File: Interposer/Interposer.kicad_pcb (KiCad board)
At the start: 2 copper layers, 55 x 52 mm, 7 parts, among them J1 Conn_01x01_Pin, J10 Conn_01x01_Pin, J11 Conn_01x01_Pin, J2 Conn_01x01_Pin

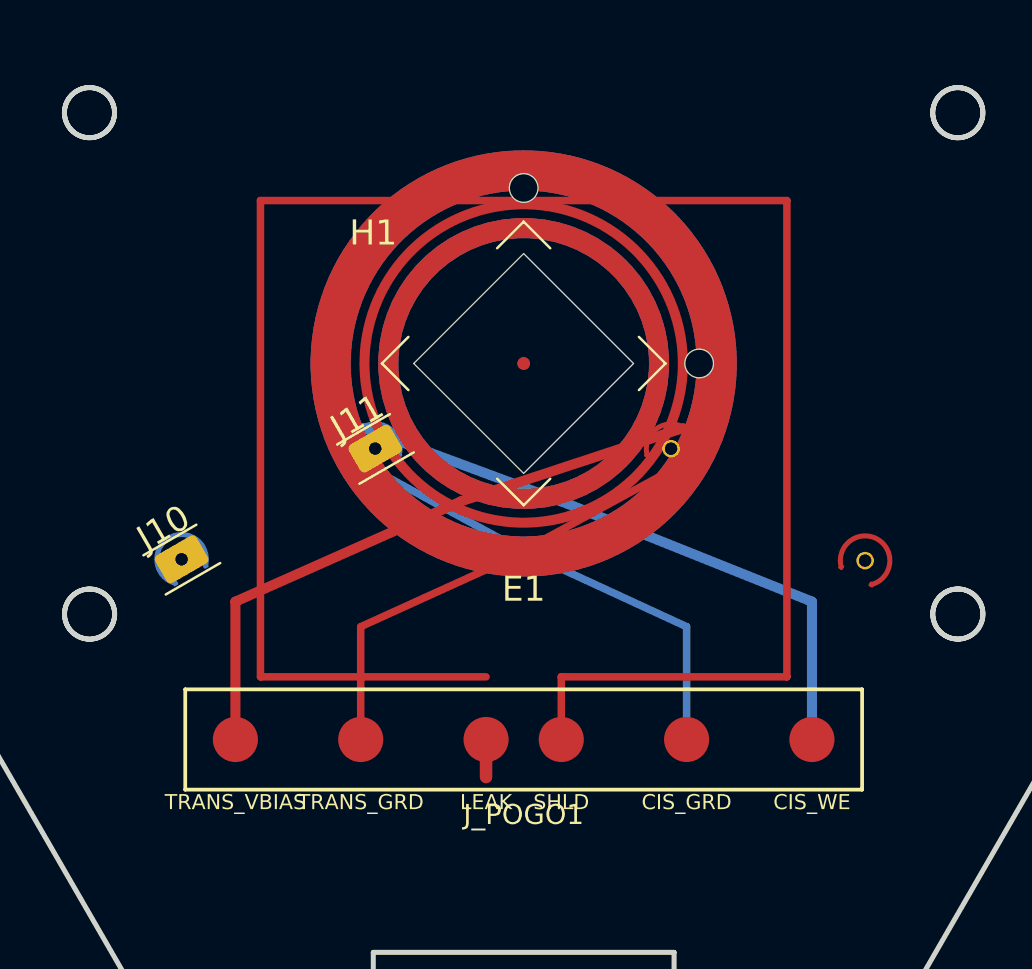
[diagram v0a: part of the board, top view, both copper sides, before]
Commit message: refactor(interposer): reconcile 4-electrode cell with channel-aligned Ag/AgCl ribbons and Gamry pinout
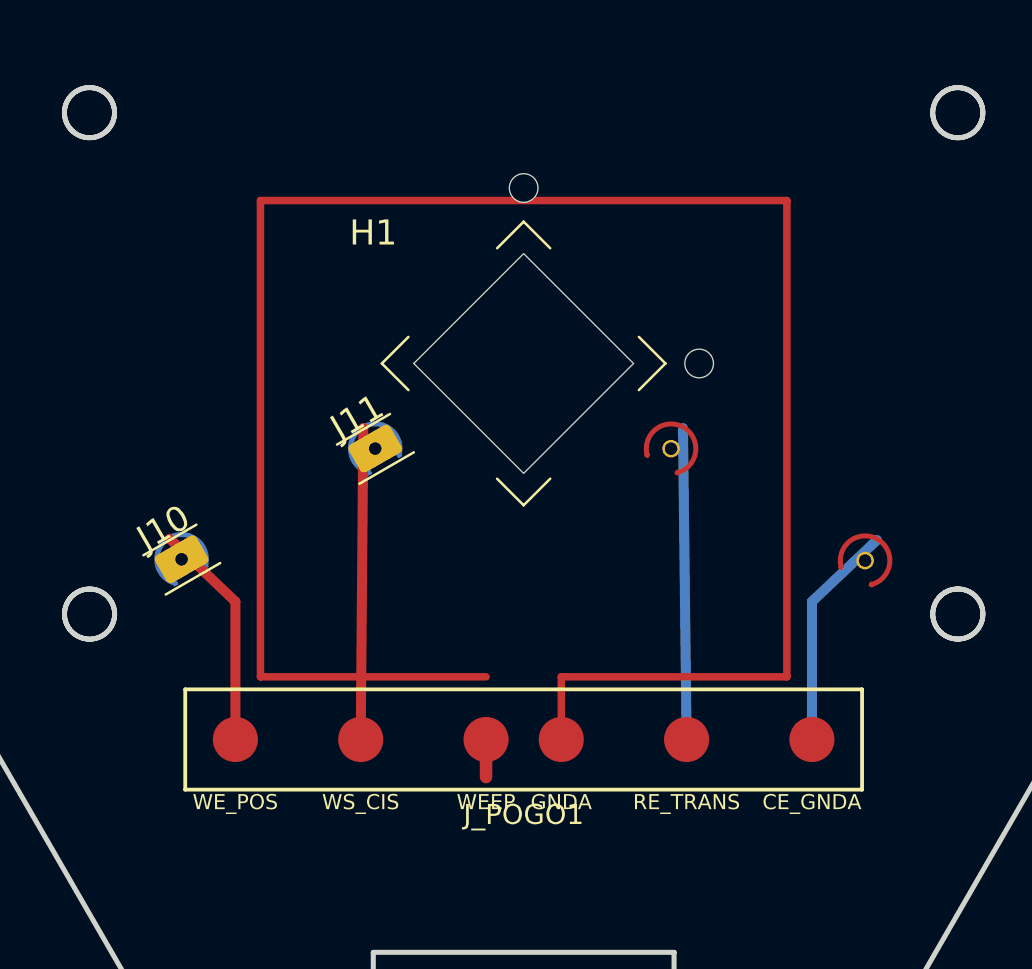
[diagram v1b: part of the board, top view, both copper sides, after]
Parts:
- removed E1: Concentric_Electrode_Cell, footprints:Concentric_Electrode_Cell
- J1: value Conn_01x01_Pin -> RE_TRANS
- J10: value Conn_01x01_Pin -> WE_POS
- J11: value Conn_01x01_Pin -> WS_CIS
- J2: value Conn_01x01_Pin -> CE_GNDA
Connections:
- J1 pad 1: >PORE_AMP -> RE_TRANS
- J1 pad 2: GUARD -> GNDA
- J10 pad 1: Vbias -> WE_POS
- J10 pad 2: GUARD_TRANS -> GNDA
- J11 pad 1: Vbias -> WS_CIS
- J11 pad 2: GUARD_TRANS -> GNDA
- J2 pad 1: >PORE_AMP -> CE_GNDA
- J2 pad 2: GUARD -> GNDA
- J_POGO1 pad 1: >PORE_AMP -> CE_GNDA
- J_POGO1 pad 2: GUARD -> RE_TRANS
- J_POGO1 pad 5: GUARD_TRANS -> WS_CIS
- J_POGO1 pad 6: Vbias -> WE_POS
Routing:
- net Vbias: track 24.7 -> 0.00 mm
- net >PORE_AMP: track 24.7 -> 0.00 mm
- net GUARD_TRANS: track 19.0 -> 0.00 mm
- net GUARD: track 18.9 -> 0.00 mm
- net WS_CIS: track 0.00 -> 12.4 mm
- net RE_TRANS: track 0.00 -> 12.4 mm
- net WE_POS: track 0.00 -> 9.13 mm
- net CE_GNDA: track 0.00 -> 9.07 mm

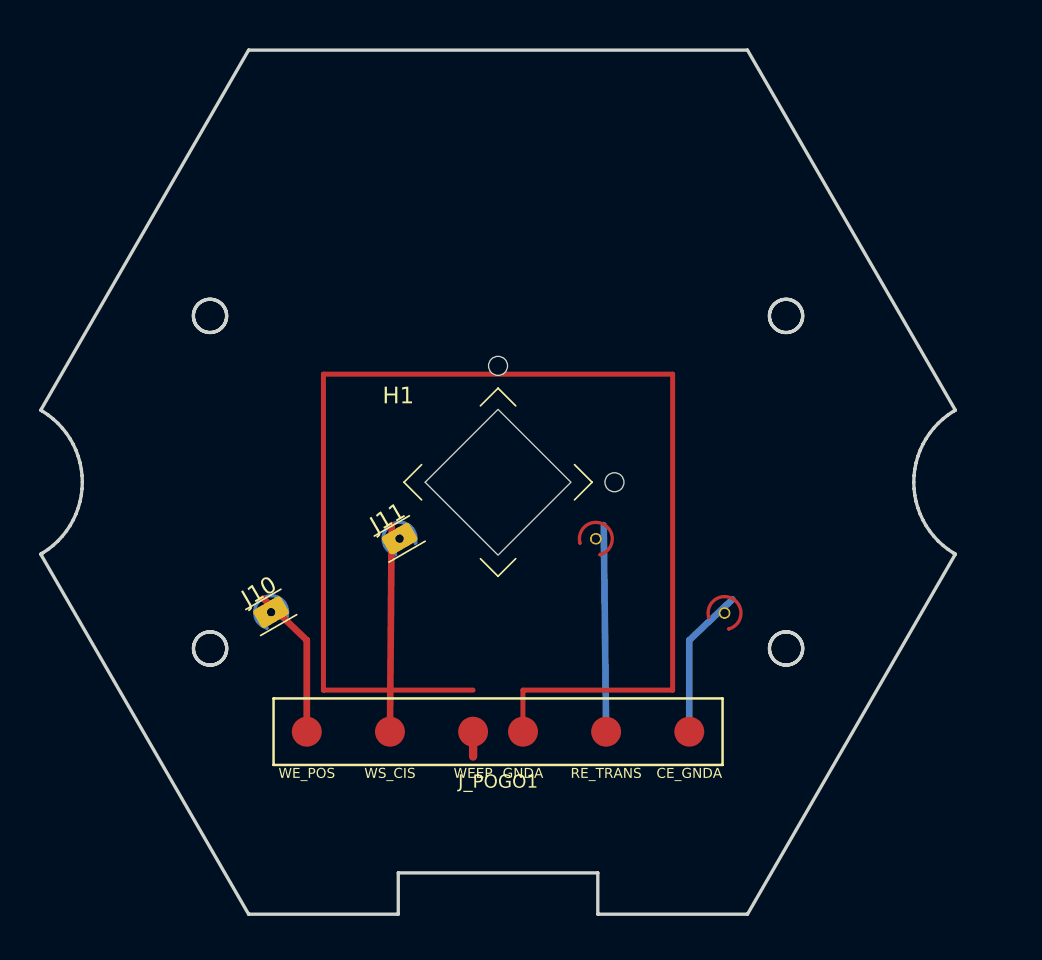
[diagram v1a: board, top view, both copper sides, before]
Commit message: feat(interposer): add full-board GNDA copper flood zones, channel-contouring weep sense moat, and interface transition vias
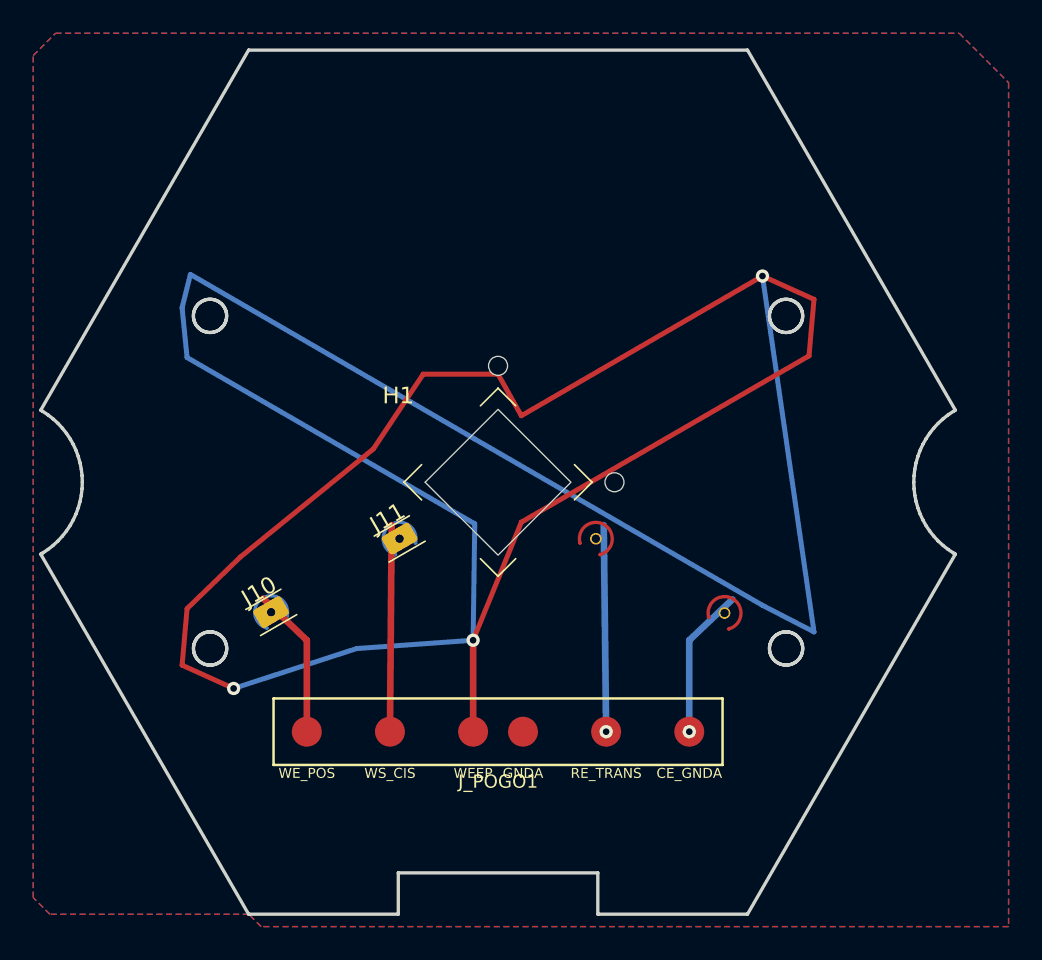
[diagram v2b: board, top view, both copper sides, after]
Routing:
- net WEEP_SENSE: track 81.0 -> 202.8 mm, vias 0 -> 3
- net RE_TRANS: vias 0 -> 1
- net CE_GNDA: vias 0 -> 1
- added copper zone on B.Cu, net GNDA
- added copper zone on F.Cu, net GNDA
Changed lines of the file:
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@@
 		(net "CE_GNDA")
 	)
-	(segment
-		(start 154 71)
-		(end 163 71)
-		(width 0.3)
-		(layer "F.Cu")
+	(via
+		(at 176 73.5)
+		(size 0.8)
+		(drill 0.4)
+		(layers "F.Cu" "B.Cu")
+		(net "CE_GNDA")
+	)
+	(via
+		(at 171 73.5)
+		(size 0.8)
+		(drill 0.4)
+		(layers "F.Cu" "B.Cu")
+		(net "RE_TRANS")
+	)
+	(via
+		(at 163 68)
+		(size 0.8)
+		(drill 0.4)
+		(layers "F.Cu" "B.Cu")
+		(net "WEEP_SENSE")
+	)
+	(via
+		(at 180.4 46.1)
+		(size 0.8)
+		(drill 0.4)
+		(layers "F.Cu" "B.Cu")
+		(net "WEEP_SENSE")
+	)
+	(via
+		(at 148.6 70.9)
+		(size 0.8)
+		(drill 0.4)
+		(layers "F.Cu" "B.Cu")
 		(net "WEEP_SENSE")
 	)
 	(segment
 		(start 163 73.5)
-		(end 163 75)
-		(width 0.5)
-		(layer "F.Cu")
-		(net "WEEP_SENSE")
-	)
-	(segment
-		(start 166 71)
-		(end 175 71)
-		(width 0.3)
-		(layer "F.Cu")
-		(net "WEEP_SENSE")
-	)
-	(segment
-		(start 166 73.5)
-		(end 166 71)
-		(width 0.3)
-		(layer "F.Cu")
-		(net "WEEP_SENSE")
-	)
-	(segment
-		(start 175 52)
-		(end 154 52)
-		(width 0.3)
-		(layer "F.Cu")
-		(net "WEEP_SENSE")
-	)
-	(segment
-		(start 175 71)
-		(end 175 52)
-		(width 0.3)
-		(layer "F.Cu")
-		(net "WEEP_SENSE")
-	)
-	(segment
-		(start 154 52)
-		(end 154 71)
-		(width 0.3)
-		(layer "F.Cu")
-		(net "WEEP_SENSE")
+		(end 163 68)
+		(width 0.4)
+		(layer "F.Cu")
+		(net "WEEP_SENSE")
+	)
+	(segment
+		(start 163 68)
+		(end 165.9 60.9)
+		(width 0.3)
+		(layer "F.Cu")
+		(net "WEEP_SENSE")
+	)
+	(segment
+		(start 165.9 60.9)
+		(end 183.2 50.9)
+		(width 0.3)
+		(layer "F.Cu")
+		(net "WEEP_SENSE")
+	)
+	(segment
+		(start 183.2 50.9)
+		(end 183.5 47.5)
+		(width 0.3)
+		(layer "F.Cu")
+		(net "WEEP_SENSE")
+	)
+	(segment
+		(start 183.5 47.5)
+		(end 180.4 46.1)
+		(width 0.3)
+		(layer "F.Cu")
+		(net "WEEP_SENSE")
+	)
+	(segment
+		(start 180.4 46.1)
+		(end 165.9 54.5)
+		(width 0.3)
+		(layer "F.Cu")
+		(net "WEEP_SENSE")
+	)
+	(segment
+		(start 165.9 54.5)
+		(end 164.5 52)
+		(width 0.3)
+		(layer "F.Cu")
+		(net "WEEP_SENSE")
+	)
+	(segment
+		(start 164.5 52)
+		(end 160 52)
+		(width 0.3)
+		(layer "F.Cu")
+		(net "WEEP_SENSE")
+	)
+	(segment
+		(start 160 52)
+		(end 157 56.5)
+		(width 0.3)
+		(layer "F.Cu")
+		(net "WEEP_SENSE")
+	)
+	(segment
+		(start 157 56.5)
+		(end 149 63)
+		(width 0.3)
+		(layer "F.Cu")
+		(net "WEEP_SENSE")
+	)
+	(segment
+		(start 149 63)
+		(end 145.8 66.1)
+		(width 0.3)
+		(layer "F.Cu")
+		(net "WEEP_SENSE")
+	)
+	(segment
+		(start 145.8 66.1)
+		(end 145.5 69.5)
+		(width 0.3)
+		(layer "F.Cu")
+		(net "WEEP_SENSE")
+	)
+	(segment
+		(start 145.5 69.5)
+		(end 148.6 70.9)
+		(width 0.3)
+		(layer "F.Cu")
+		(net "WEEP_SENSE")
+	)
+	(segment
+		(start 148.6 70.9)
+		(end 156 68.5)
+		(width 0.3)
+		(layer "B.Cu")
+		(net "WEEP_SENSE")
+	)
+	(segment
+		(start 156 68.5)
+		(end 163 68)
+		(width 0.3)
+		(layer "B.Cu")
+		(net "WEEP_SENSE")
+	)
+	(segment
+		(start 163 68)
+		(end 163.1 61)
+		(width 0.3)
+		(layer "B.Cu")
+		(net "WEEP_SENSE")
+	)
+	(segment
+		(start 163.1 61)
+		(end 145.8 51)
+		(width 0.3)
+		(layer "B.Cu")
+		(net "WEEP_SENSE")
+	)
+	(segment
+		(start 145.8 51)
+		(end 145.5 48)
+		(width 0.3)
+		(layer "B.Cu")
+		(net "WEEP_SENSE")
+	)
+	(segment
+		(start 145.5 48)
+		(end 146 46)
+		(width 0.3)
+		(layer "B.Cu")
+		(net "WEEP_SENSE")
+	)
+	(segment
+		(start 146 46)
+		(end 163.1 55.9)
+		(width 0.3)
+		(layer "B.Cu")
+		(net "WEEP_SENSE")
+	)
+	(segment
+		(start 163.1 55.9)
+		(end 180.4 65.9)
+		(width 0.3)
+		(layer "B.Cu")
+		(net "WEEP_SENSE")
+	)
+	(segment
+		(start 180.4 65.9)
+		(end 183.5 67.5)
+		(width 0.3)
+		(layer "B.Cu")
+		(net "WEEP_SENSE")
+	)
+	(segment
+		(start 183.5 67.5)
+		(end 180.4 46.1)
+		(width 0.3)
+		(layer "B.Cu")
+		(net "WEEP_SENSE")
+	)
+	(zone
+		(net "GNDA")
+		(layers "F.Cu" "B.Cu")
+		(hatch edge 0.5)
+		(connect_pads
+			(clearance 0.25)
+		)
+		(min_thickness 0.2)
+		(fill yes
+			(thermal_gap 0.3)
+			(thermal_bridge_width 0.3)
+			(island_removal_mode 0)
+		)
+		(polygon
+			(pts
+				(xy 149.51 84.48) (xy 137.55 84.48) (xy 136.55 83.48) (xy 136.55 32.84) (xy 137.89 31.5) (xy 192.23 31.5)
+				(xy 195.2 34.47) (xy 195.2 85.22) (xy 150.25 85.22)
+			)
+		)
 	)
 	(embedded_fonts no)

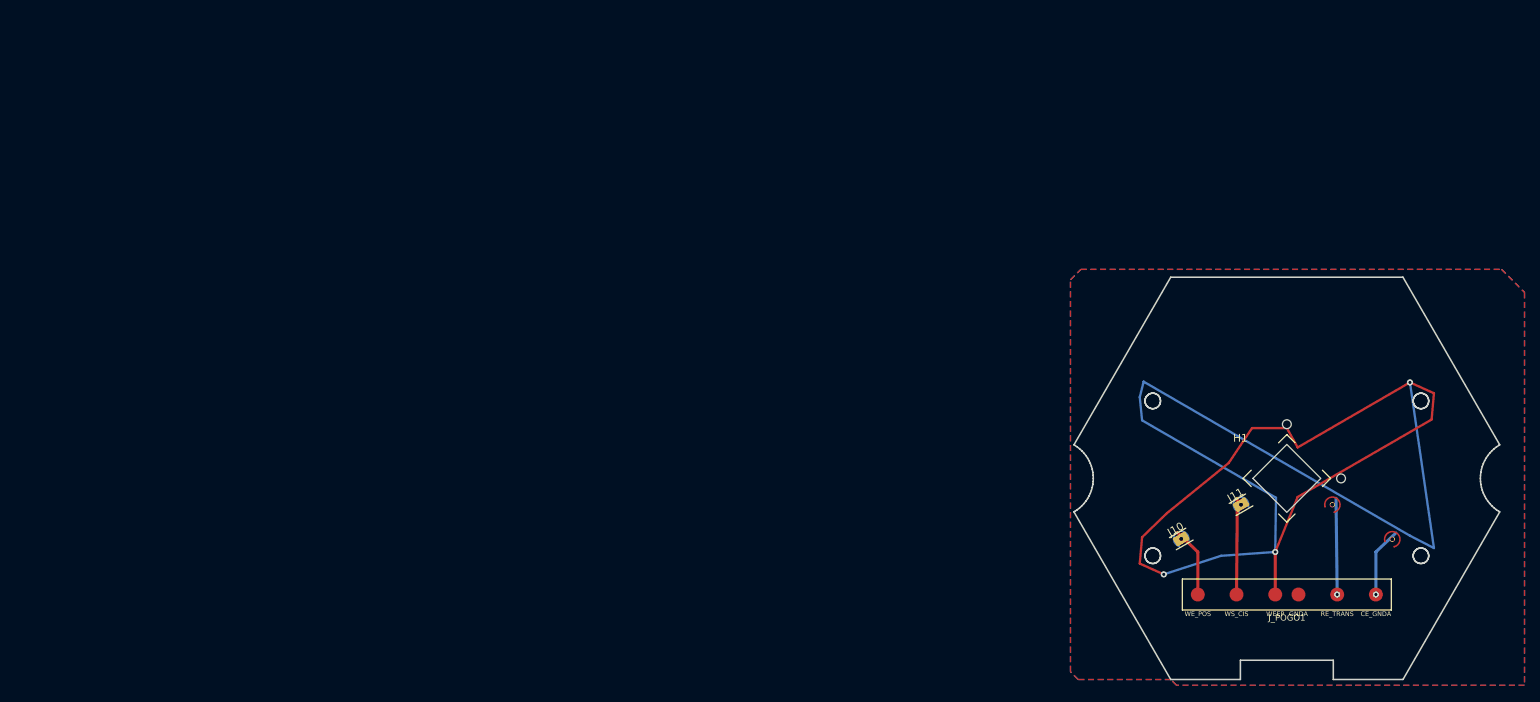
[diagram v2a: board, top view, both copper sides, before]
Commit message: Update Interposer and Amplifier interfaces to 12-pin Guarded Pogo layout
Modifies `J_POGO1` (the mechanical interface bridging the active amplifier and
passive flowcell interposer) from a 6-pin linear array to a 12-pin layout.

This 12-pin architecture surrounds the ultra-high impedance signals (`WS_CIS`
and `RE_TRANS`) with explicitly driven `GUARD` pins. By flanking these sensitive
nodes with driven low-impedance guards across the mechanical pogo connection,
stray surface leakage across the FR4 and mating interfaces is intercepted and
bootstrapped.

Changes:
- Replaced 6-pin target array footprints with `PogoPin_Target_12Pin_Distributed`.
- Replaced 6-pin spring header footprints with `PogoPin_SpringHeader_12Pin_Distributed`.
- Updated KiCad footprint `.kicad_mod` files to feature 12 pads.
- Updated `scripts/build_interposer_kicad.py` to instantiate the new 12-pin generic connector symbols and bind to the correct footprints.
- Updated unit test assertions in `tests/test_interposer_kicad.py` to expect the new pin counts, names, and symbol mappings.

Co-authored-by: google-labs-jules[bot] <161369871+google-labs-jules[bot]@users.noreply.github.com>
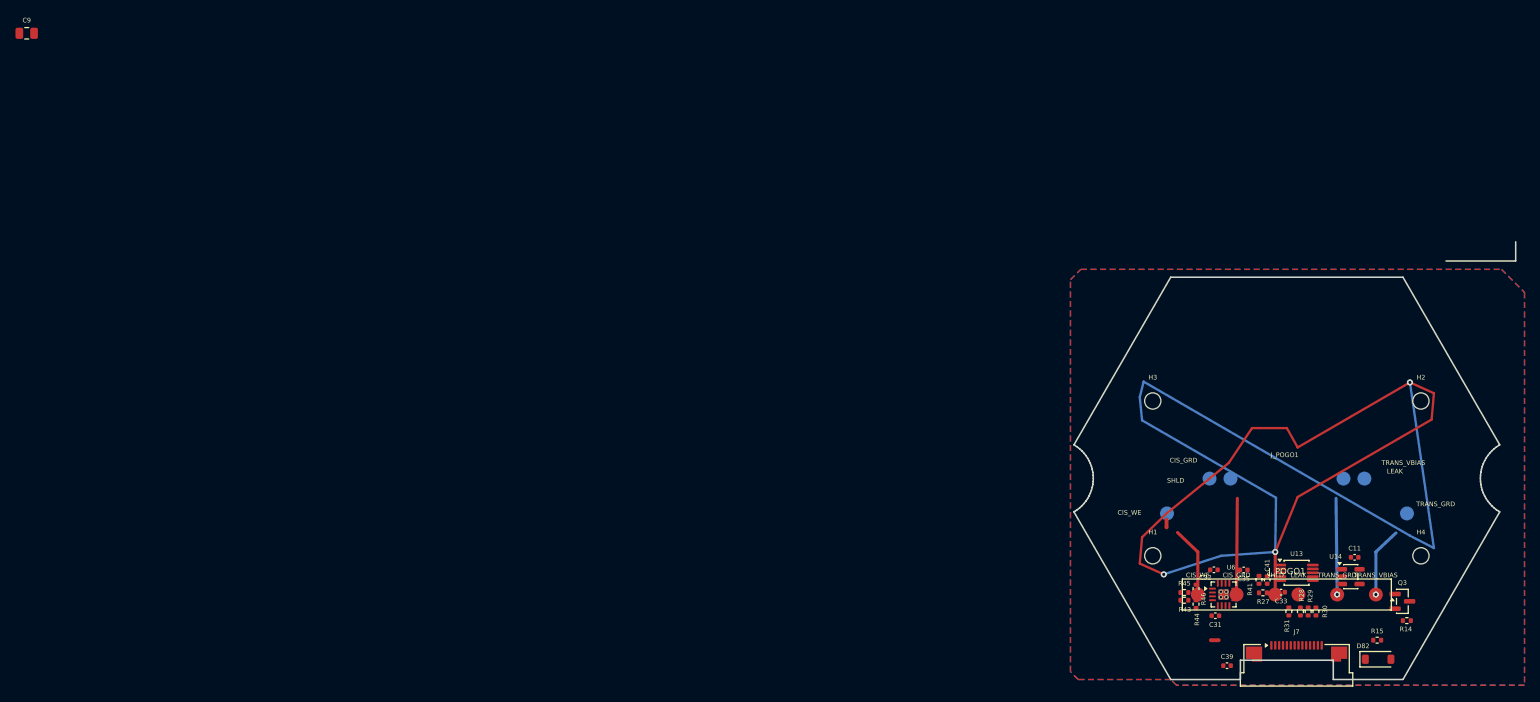
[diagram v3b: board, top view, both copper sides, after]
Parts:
- removed J1: RE_TRANS, footprints:Electrode_Guard_Shield
- removed J10: WE_POS, footprints:Electrode_Guard_Shield
- removed J11: WS_CIS, footprints:Electrode_Guard_Shield
- removed J2: CE_GNDA, footprints:Electrode_Guard_Shield
- removed the J_POGO1 at (164.5, 73.5)
- added C11: 4.7u, Capacitor_SMD:C_0402_1005Metric, F.Cu at (173.3, 68.7)
- added C31: 100nF, Capacitor_SMD:C_0402_1005Metric, F.Cu at (155.3, 76.2)
- added C32: 100nF, Capacitor_SMD:C_0402_1005Metric, F.Cu at (155.1, 70.3)
- added C33: 100nF, Capacitor_SMD:C_0402_1005Metric, F.Cu at (163.8, 73.2)
- added C35: 10u, Capacitor_SMD:C_0402_1005Metric, F.Cu at (158.9, 70.3)
- added C39: 100nF, Capacitor_SMD:C_0402_1005Metric, F.Cu at (156.8, 82.7)
- added C41: 1nF, Capacitor_SMD:C_0402_1005Metric, F.Cu at (162.0, 71.6)
- added C9: 100nF, Capacitor_SMD:C_0805_2012Metric, F.Cu at (1.73, 1.00)
- added D82: MBR0540, Diode_SMD:D_SOD-123, F.Cu at (176.3, 81.9)
- added H2: FluidHole, MountingHole:MountingHole_2.1mm, F.Cu at (181.8, 48.5)
- added H3: FluidHole, MountingHole:MountingHole_2.1mm, F.Cu at (147.2, 48.5)
- added H4: FluidHole, MountingHole:MountingHole_2.1mm, F.Cu at (181.8, 68.5)
- added J7: Conn_01x14_MountingPin, Connector_FFC-FPC:Amphenol_F32R-1A7x1-11014_1x14-1MP_P0.5mm_Horizontal, F.Cu at (165.8, 83.0)
- added J_POGO1: PogoPin_SpringHeader_6Pin_Array, footprints:PogoPin_Target_6Pin_Distributed, F.Cu at (164.5, 58.5)
- added J_POGO1: PogoPin_Target_12Pin_Distributed, footprints:PogoPin_Target_12Pin_Distributed, F.Cu at (164.5, 73.5)
- added NT7: NetTie_2, NetTie:NetTie-2_SMD_Pad0.5mm, F.Cu at (155.2, 79.4)
- added NT8: NetTie_2, NetTie:NetTie-2_SMD_Pad0.5mm, F.Cu at (149.0, 64.3)
- added Q3: 2N7002, Package_TO_SOT_SMD:SOT-23, F.Cu at (179.4, 74.4)
- added R14: 100k, Resistor_SMD:R_0402_1005Metric, F.Cu at (180.0, 76.9)
- added R15: 100k, Resistor_SMD:R_0402_1005Metric, F.Cu at (176.2, 79.4)
- added R27: 27, Resistor_SMD:R_0402_1005Metric, F.Cu at (161.4, 73.3)
- added R28: 49.9, Resistor_SMD:R_0402_1005Metric, F.Cu at (166.3, 75.7)
- added R29: 49.9, Resistor_SMD:R_0402_1005Metric, F.Cu at (167.3, 75.7)
- added R30: 49.9, Resistor_SMD:R_0402_1005Metric, F.Cu at (168.3, 75.7)
- added R31: 49.9, Resistor_SMD:R_0402_1005Metric, F.Cu at (164.8, 75.7)
- added R41: 27, Resistor_SMD:R_0402_1005Metric, F.Cu at (160.9, 71.6)
- added R43: 499 (0.1%), Resistor_SMD:R_0402_1005Metric, F.Cu at (151.3, 74.2)
- added R44: 499 (0.1%), Resistor_SMD:R_0402_1005Metric, F.Cu at (152.8, 74.7)
- added R45: 499 (0.1%), Resistor_SMD:R_0402_1005Metric, F.Cu at (151.3, 73.2)
- added R46: 499 (0.1%), Resistor_SMD:R_0402_1005Metric, F.Cu at (152.8, 72.7)
- added U13: AD40xxBRMZ, Package_SO:MSOP-10_3x3mm_P0.5mm, F.Cu at (165.8, 70.7)
- added U14: LP5907MFX-1.8, Package_TO_SOT_SMD:SOT-23-5, F.Cu at (172.8, 71.2)
- added U6: ADA4940-1xCP, Package_CSP:LFCSP-16-1EP_3x3mm_P0.5mm_EP1.3x1.3mm_ThermalVias, F.Cu at (156.3, 73.5)
- H1: value Nanopore -> FluidHole; footprint footprints:Nanopore holder_recessed -> MountingHole:MountingHole_2.1mm
- moved H1 20.0 mm to (147.2, 68.5)
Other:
- board size 55 x 52 mm -> 57.1 x 56.5 mm
